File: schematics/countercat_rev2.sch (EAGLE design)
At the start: 59 parts, among them Q1 IRF520, Q3 IRF520, Q4 IRF520, Q5 IRF520, U4 ATMEGA328P, Y1 16MHz

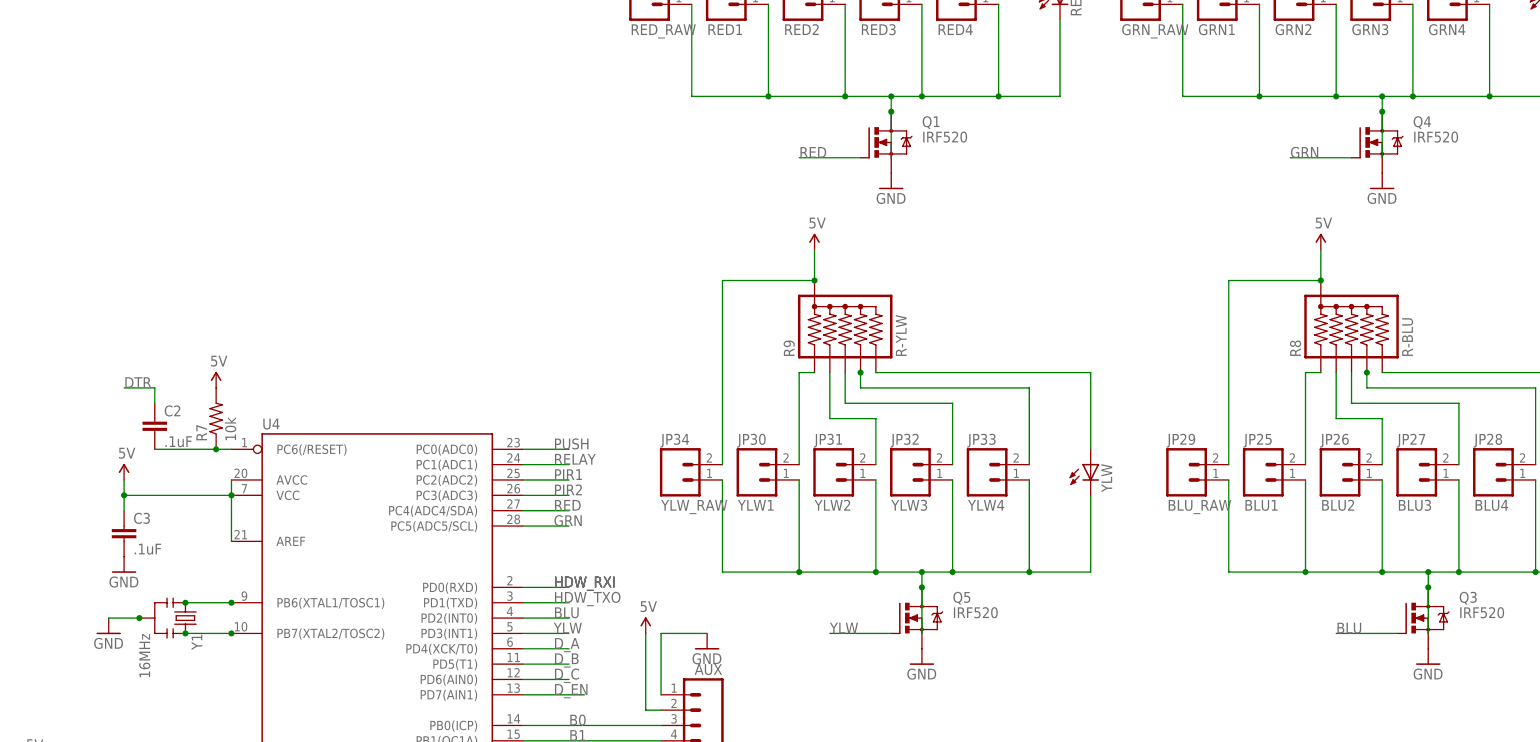
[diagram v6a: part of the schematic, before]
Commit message: Fixed error with shorted DTR net in schematic
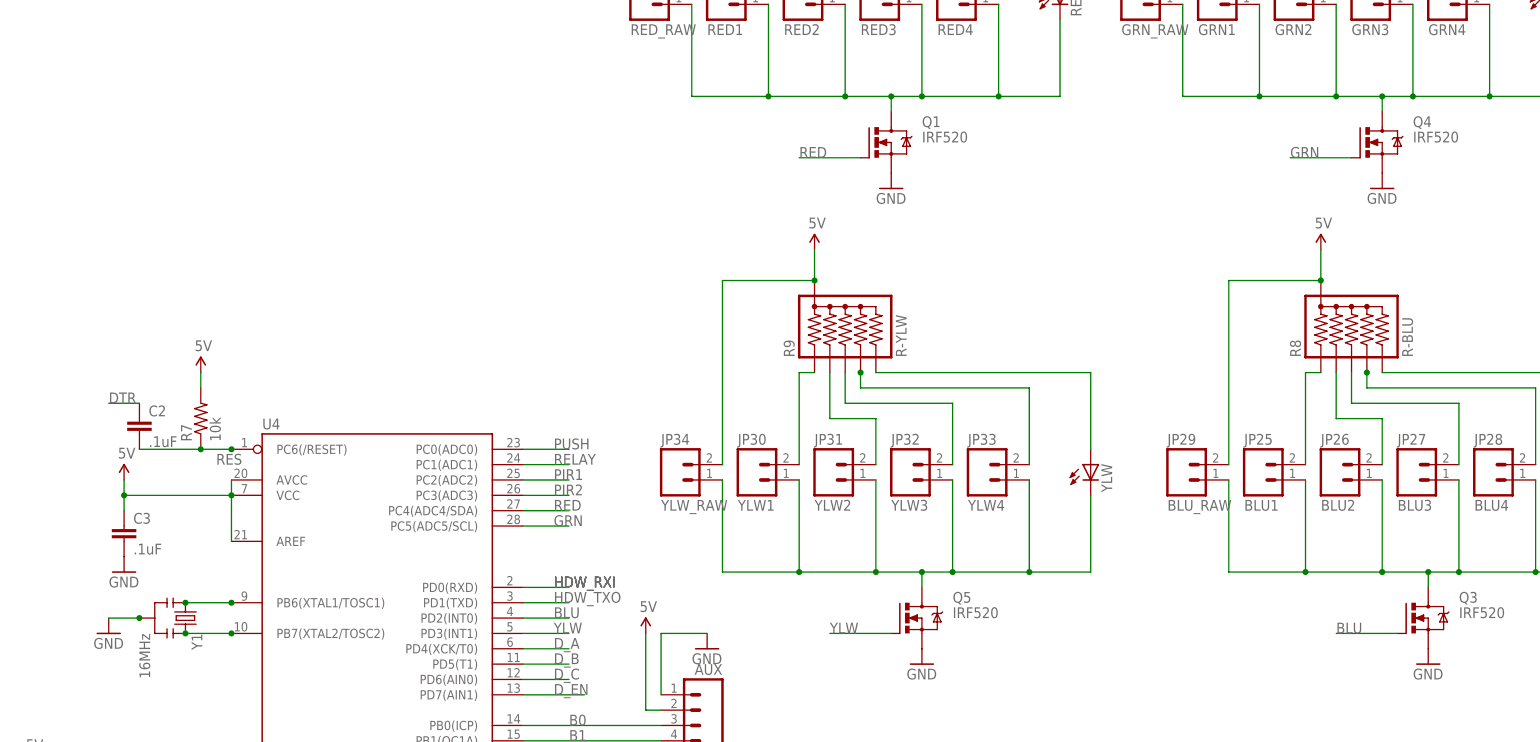
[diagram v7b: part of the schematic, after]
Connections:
- new net RES: C2.2, R7.1, U4.PC6(/RESET)
- net DTR: no longer C2.2, R7.1, U4.PC6(/RESET)
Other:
- moved on the sheet: C2, R7
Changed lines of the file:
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@@
 <instance part="Y1" gate="G$1" x="-53.34" y="45.72" rot="R270"/>
 <instance part="GND7" gate="1" x="-66.04" y="43.18"/>
-<instance part="C2" gate="G$1" x="-58.42" y="76.2"/>
-<instance part="R7" gate="G$1" x="-48.26" y="78.74" rot="R90"/>
-<instance part="U$8" gate="G$1" x="-48.26" y="83.82"/>
+<instance part="C2" gate="G$1" x="-60.96" y="76.2"/>
+<instance part="R7" gate="G$1" x="-50.8" y="78.74" rot="R90"/>
+<instance part="U$8" gate="G$1" x="-50.8" y="86.36"/>
 <instance part="C3" gate="G$1" x="-63.5" y="58.42"/>
 <instance part="GND9" gate="1" x="-63.5" y="53.34"/>
@@
 <pinref part="R7" gate="G$1" pin="2"/>
 <pinref part="U$8" gate="G$1" pin="5V"/>
+<wire x1="-50.8" y1="83.82" x2="-50.8" y2="86.36" width="0.1524" layer="91"/>
 </segment>
 <segment>
@@
 <net name="DTR" class="0">
 <segment>
-<wire x1="-45.72" y1="73.66" x2="-48.26" y2="73.66" width="0.1524" layer="91"/>
-<wire x1="-48.26" y1="73.66" x2="-58.42" y2="73.66" width="0.1524" layer="91"/>
-<junction x="-48.26" y="73.66"/>
-<pinref part="C2" gate="G$1" pin="2"/>
-<pinref part="R7" gate="G$1" pin="1"/>
-<pinref part="U4" gate="G$1" pin="PC6(/RESET)"/>
-</segment>
-<segment>
-<wire x1="-58.42" y1="81.28" x2="-58.42" y2="83.82" width="0.1524" layer="91"/>
-<wire x1="-58.42" y1="83.82" x2="-63.5" y2="83.82" width="0.1524" layer="91"/>
-<label x="-63.5" y="83.82" size="1.778" layer="95"/>
-<pinref part="C2" gate="G$1" pin="1"/>
-</segment>
-<segment>
 <wire x1="-119.38" y1="66.04" x2="-111.76" y2="66.04" width="0.1524" layer="91"/>
 <label x="-111.76" y="66.04" size="1.778" layer="95"/>
 <pinref part="JP6" gate="G$1" pin="1"/>
+</segment>
+<segment>
+<pinref part="C2" gate="G$1" pin="1"/>
+<wire x1="-60.96" y1="81.28" x2="-66.04" y2="81.28" width="0.1524" layer="91"/>
+<label x="-66.04" y="81.28" size="1.778" layer="95"/>
 </segment>
 </net>
@@
 <junction x="149.86" y="132.08"/>
 <pinref part="JP24" gate="G$1" pin="1"/>
-<wire x1="144.78" y1="129.54" x2="144.78" y2="121.92" width="0.1524" layer="91"/>
 <wire x1="111.76" y1="147.32" x2="111.76" y2="132.08" width="0.1524" layer="91"/>
 <wire x1="111.76" y1="132.08" x2="124.46" y2="132.08" width="0.1524" layer="91"/>
 <pinref part="Q4" gate="G$1" pin="D"/>
-<junction x="144.78" y="129.54"/>
 <wire x1="162.56" y1="132.08" x2="172.72" y2="132.08" width="0.1524" layer="91"/>
 <pinref part="GRN" gate="G$1" pin="C"/>
@@
 <junction x="68.58" y="132.08"/>
 <pinref part="JP10" gate="G$1" pin="1"/>
-<wire x1="63.5" y1="129.54" x2="63.5" y2="121.92" width="0.1524" layer="91"/>
 <wire x1="30.48" y1="147.32" x2="30.48" y2="132.08" width="0.1524" layer="91"/>
 <wire x1="30.48" y1="132.08" x2="43.18" y2="132.08" width="0.1524" layer="91"/>
 <pinref part="Q1" gate="G$1" pin="D"/>
-<junction x="63.5" y="129.54"/>
 <wire x1="81.28" y1="132.08" x2="91.44" y2="132.08" width="0.1524" layer="91"/>
 <pinref part="RED" gate="G$1" pin="C"/>
@@
 <junction x="157.48" y="53.34"/>
 <pinref part="JP29" gate="G$1" pin="1"/>
-<wire x1="152.4" y1="50.8" x2="152.4" y2="43.18" width="0.1524" layer="91"/>
 <wire x1="119.38" y1="68.58" x2="119.38" y2="53.34" width="0.1524" layer="91"/>
 <wire x1="119.38" y1="53.34" x2="132.08" y2="53.34" width="0.1524" layer="91"/>
 <pinref part="Q3" gate="G$1" pin="D"/>
-<junction x="152.4" y="50.8"/>
 <wire x1="170.18" y1="53.34" x2="180.34" y2="53.34" width="0.1524" layer="91"/>
 <pinref part="BLU" gate="G$1" pin="C"/>
@@
 <junction x="73.66" y="53.34"/>
 <pinref part="JP34" gate="G$1" pin="1"/>
-<wire x1="68.58" y1="50.8" x2="68.58" y2="43.18" width="0.1524" layer="91"/>
 <wire x1="35.56" y1="68.58" x2="35.56" y2="53.34" width="0.1524" layer="91"/>
 <wire x1="35.56" y1="53.34" x2="48.26" y2="53.34" width="0.1524" layer="91"/>
 <pinref part="Q5" gate="G$1" pin="D"/>
-<junction x="68.58" y="50.8"/>
 <wire x1="86.36" y1="53.34" x2="96.52" y2="53.34" width="0.1524" layer="91"/>
 <pinref part="YLW" gate="G$1" pin="C"/>
@@
 </segment>
 </net>
+<net name="RES" class="0">
+<segment>
+<wire x1="-50.8" y1="73.66" x2="-60.96" y2="73.66" width="0.1524" layer="91"/>
+<pinref part="C2" gate="G$1" pin="2"/>
+<pinref part="R7" gate="G$1" pin="1"/>
+<junction x="-50.8" y="73.66"/>
+<pinref part="U4" gate="G$1" pin="PC6(/RESET)"/>
+<wire x1="-50.8" y1="73.66" x2="-45.72" y2="73.66" width="0.1524" layer="91"/>
+<junction x="-45.72" y="73.66"/>
+<label x="-48.26" y="71.12" size="1.778" layer="95"/>
+</segment>
+</net>
